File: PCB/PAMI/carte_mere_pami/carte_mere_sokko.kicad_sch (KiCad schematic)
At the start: 36 parts, among them IC1 ESP32-S3-WROOM-1-N16R8, IC2 LDO_3.3V_bis, J1 Conn_01x08_Socket, J10 Conn_01x07_Socket, J11 Conn_01x07_Socket, J12 Conn_Servos, J13 Unused GPIO Pins, J14 LiDAR Connector, J2 Connector 5V, J3 Connector 3.3V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

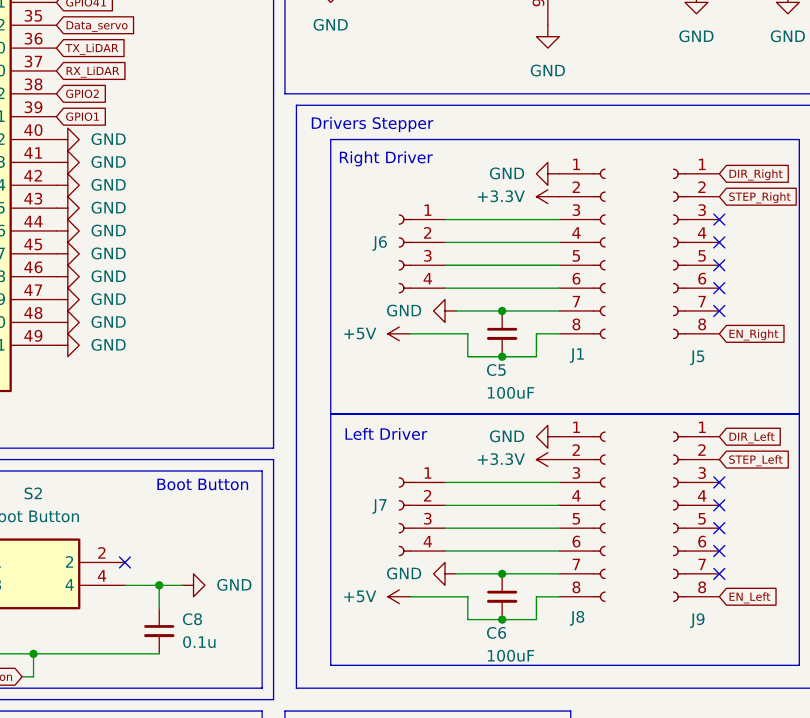
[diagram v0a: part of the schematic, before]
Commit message: PCB PAMI Nearly done, lack ground plane
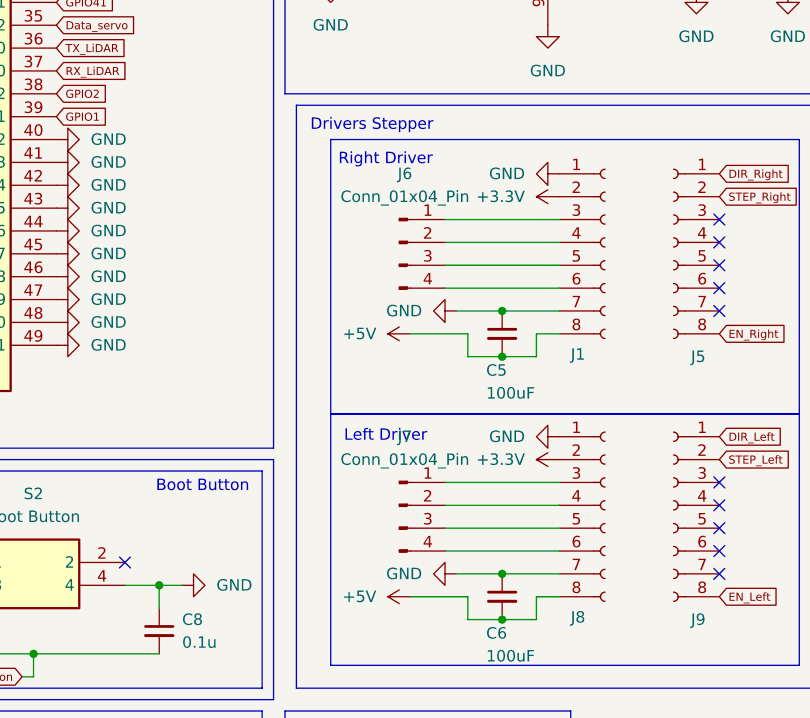
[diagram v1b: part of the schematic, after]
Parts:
- removed J6, J7: Conn_01x04_Socket, Connector_PinHeader_2.54mm:PinHeader_1x04_P2.54mm_Vertical, symbol Connector:Conn_01x04_Socket
- added J6, J7: Conn_01x04_Pin, Connector_JST:JST_XH_B4B-XH-A_1x04_P2.50mm_Vertical, symbol Connector:Conn_01x04_Pin
- J13: now left out of the parts list
- R2: footprint (none) -> Resistor_SMD:R_0805_2012Metric_Pad1.20x1.40mm_HandSolder
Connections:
- net at J8.3 (Pin_3): now also J7.1 (Pin_1)
- net at J8.4 (Pin_4): now also J7.2 (Pin_2)
- net at J8.5 (Pin_5): now also J7.3 (Pin_3)
- net at J8.6 (Pin_6): now also J7.4 (Pin_4)
- net at J1.3 (Pin_3): now also J6.1 (Pin_1)
- net at J1.4 (Pin_4): now also J6.2 (Pin_2)
- net at J1.5 (Pin_5): now also J6.3 (Pin_3)
- net at J1.6 (Pin_6): now also J6.4 (Pin_4)
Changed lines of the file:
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@@
 		(unit 1)
 		(exclude_from_sim no)
-		(in_bom yes)
-		(on_board yes)
+		(in_bom no)
+		(on_board no)
 		(dnp no)
 		(property "Reference" "J13"
@@
 	)
 	(symbol
-		(lib_id "Connector:Conn_01x04_Socket")
-		(at 378.46 137.16 0)
-		(mirror y)
+		(lib_id "power:GND")
+		(at 148.59 203.2 0)
 		(unit 1)
 		(exclude_from_sim no)
@@
 		(on_board yes)
 		(dnp no)
-		(property "Reference" "J6"
-			(at 377.19 137.1599 0)
+		(property "Reference" "#PWR023"
+			(at 148.59 209.55 0)
 			(effects
 				(font
 					(size 1.27 1.27)
 				)
-				(justify left)
+				(hide yes)
 			)
 		)
-		(property "Value" "Conn_01x04_Socket"
-			(at 377.19 139.6999 0)
+		(property "Value" "GND"
+			(at 149.098 207.772 0)
 			(effects
 				(font
 					(size 1.27 1.27)
 				)
-				(justify left)
-				(hide yes)
 			)
 		)
-		(property "Footprint" "Connector_PinHeader_2.54mm:PinHeader_1x04_P2.54mm_Vertical"
-			(at 378.46 137.16 0)
+		(property "Footprint" ""
+			(at 148.59 203.2 0)
 			(effects
 				(font
@@
 			)
 		)
-		(property "Datasheet" "~"
-			(at 378.46 137.16 0)
+		(property "Datasheet" ""
+			(at 148.59 203.2 0)
 			(effects
 				(font
@@
 			)
 		)
-		(property "Description" "Generic connector, single row, 01x04, script generated"
-			(at 378.46 137.16 0)
+		(property "Description" "Power symbol creates a global label with name \"GND\" , ground"
+			(at 148.59 203.2 0)
 			(effects
 				(font
@@
 			)
 		)
-		(pin "2"
-		)
-		(pin "4"
-		)
-		(pin "3"
-		)
 		(pin "1"
 		)
 		(instances
-			(project ""
+			(project "carte_mere_sokko"
 				(path "/dee43b08-90b1-40b6-8660-52baa7e8ef70"
-					(reference "J6")
+					(reference "#PWR023")
 					(unit 1)
 				)
@@
 	)
 	(symbol
-		(lib_id "power:GND")
-		(at 148.59 203.2 0)
+		(lib_id "power:+3.3V")
+		(at 396.24 132.08 90)
 		(unit 1)
 		(exclude_from_sim no)
@@
 		(on_board yes)
 		(dnp no)
-		(property "Reference" "#PWR023"
-			(at 148.59 209.55 0)
+		(fields_autoplaced yes)
+		(property "Reference" "#PWR013"
+			(at 400.05 132.08 0)
 			(effects
 				(font
@@
 			)
 		)
-		(property "Value" "GND"
-			(at 149.098 207.772 0)
+		(property "Value" "+3.3V"
+			(at 392.43 132.0799 90)
 			(effects
 				(font
 					(size 1.27 1.27)
 				)
+				(justify left)
 			)
 		)
 		(property "Footprint" ""
-			(at 148.59 203.2 0)
+			(at 396.24 132.08 0)
 			(effects
 				(font
@@
 		)
 		(property "Datasheet" ""
-			(at 148.59 203.2 0)
+			(at 396.24 132.08 0)
 			(effects
 				(font
@@
 			)
 		)
-		(property "Description" "Power symbol creates a global label with name \"GND\" , ground"
-			(at 148.59 203.2 0)
+		(property "Description" "Power symbol creates a global label with name \"+3.3V\""
+			(at 396.24 132.08 0)
 			(effects
 				(font
@@
 			(project "carte_mere_sokko"
 				(path "/dee43b08-90b1-40b6-8660-52baa7e8ef70"
-					(reference "#PWR023")
+					(reference "#PWR013")
 					(unit 1)
 				)
@@
 	)
 	(symbol
-		(lib_id "power:+3.3V")
-		(at 396.24 132.08 90)
+		(lib_id "Connector:Conn_01x04_Pin")
+		(at 378.46 166.37 0)
 		(unit 1)
 		(exclude_from_sim no)
@@
 		(dnp no)
 		(fields_autoplaced yes)
-		(property "Reference" "#PWR013"
-			(at 400.05 132.08 0)
+		(property "Reference" "J7"
+			(at 379.095 158.75 0)
 			(effects
 				(font
 					(size 1.27 1.27)
 				)
-				(hide yes)
 			)
 		)
-		(property "Value" "+3.3V"
-			(at 392.43 132.0799 90)
+		(property "Value" "Conn_01x04_Pin"
+			(at 379.095 161.29 0)
 			(effects
 				(font
 					(size 1.27 1.27)
 				)
-				(justify left)
 			)
 		)
-		(property "Footprint" ""
-			(at 396.24 132.08 0)
+		(property "Footprint" "Connector_JST:JST_XH_B4B-XH-A_1x04_P2.50mm_Vertical"
+			(at 378.46 166.37 0)
 			(effects
 				(font
@@
 			)
 		)
-		(property "Datasheet" ""
-			(at 396.24 132.08 0)
+		(property "Datasheet" "~"
+			(at 378.46 166.37 0)
 			(effects
 				(font
@@
 			)
 		)
-		(property "Description" "Power symbol creates a global label with name \"+3.3V\""
-			(at 396.24 132.08 0)
+		(property "Description" "Generic connector, single row, 01x04, script generated"
+			(at 378.46 166.37 0)
 			(effects
 				(font
@@
 		(pin "1"
 		)
+		(pin "2"
+		)
+		(pin "3"
+		)
+		(pin "4"
+		)
 		(instances
-			(project "carte_mere_sokko"
+			(project ""
 				(path "/dee43b08-90b1-40b6-8660-52baa7e8ef70"
-					(reference "#PWR013")
+					(reference "J7")
 					(unit 1)
 				)
@@
 	)
 	(symbol
+		(lib_id "Connector:Conn_01x04_Pin")
+		(at 378.46 137.16 0)
+		(unit 1)
+		(exclude_from_sim no)
+		(in_bom yes)
+		(on_board yes)
+		(dnp no)
+		(fields_autoplaced yes)
+		(property "Reference" "J6"
+			(at 379.095 129.54 0)
+			(effects
+				(font
+					(size 1.27 1.27)
+				)
+			)
+		)
+		(property "Value" "Conn_01x04_Pin"
+			(at 379.095 132.08 0)
+			(effects
+				(font
+					(size 1.27 1.27)
+				)
+			)
+		)
+		(property "Footprint" "Connector_JST:JST_XH_B4B-XH-A_1x04_P2.50mm_Vertical"
+			(at 378.46 137.16 0)
+			(effects
+				(font
+					(size 1.27 1.27)
+				)
+				(hide yes)
+			)
+		)
+		(property "Datasheet" "~"
+			(at 378.46 137.16 0)
+			(effects
+				(font
+					(size 1.27 1.27)
+				)
+				(hide yes)
+			)
+		)
+		(property "Description" "Generic connector, single row, 01x04, script generated"
+			(at 378.46 137.16 0)
+			(effects
+				(font
+					(size 1.27 1.27)
+				)
+				(hide yes)
+			)
+		)
+		(pin "2"
+		)
+		(pin "4"
+		)
+		(pin "3"
+		)
+		(pin "1"
+		)
+		(instances
+			(project ""
+				(path "/dee43b08-90b1-40b6-8660-52baa7e8ef70"
+					(reference "J6")
+					(unit 1)
+				)
+			)
+		)
+	)
+	(symbol
 		(lib_id "power:GND")
 		(at 384.81 144.78 270)
@@
 			)
 		)
-		(property "Footprint" ""
+		(property "Footprint" "Resistor_SMD:R_0805_2012Metric_Pad1.20x1.40mm_HandSolder"
 			(at 285.242 109.22 90)
 			(effects
@@
 					(unit 1)
 				)
-			)
-		)
-	)
-	(symbol
-		(lib_id "Connector:Conn_01x04_Socket")
-		(at 378.46 166.37 0)
-		(mirror y)
-		(unit 1)
-		(exclude_from_sim no)
-		(in_bom yes)
-		(on_board yes)
-		(dnp no)
-		(property "Reference" "J7"
-			(at 377.19 166.3699 0)
-			(effects
-				(font
-					(size 1.27 1.27)
-				)
-				(justify left)
-			)
-		)
-		(property "Value" "Conn_01x04_Socket"
-			(at 377.19 168.9099 0)
-			(effects
-				(font
-					(size 1.27 1.27)
-				)
-				(justify left)
-				(hide yes)
-			)
-		)
-		(property "Footprint" "Connector_PinHeader_2.54mm:PinHeader_1x04_P2.54mm_Vertical"
-			(at 378.46 166.37 0)
-			(effects
-				(font
-					(size 1.27 1.27)
-				)
-				(hide yes)
-			)
-		)
-		(property "Datasheet" "~"
-			(at 378.46 166.37 0)
-			(effects
-				(font
-					(size 1.27 1.27)
-				)
-				(hide yes)
-			)
-		)
-		(property "Description" "Generic connector, single row, 01x04, script generated"
-			(at 378.46 166.37 0)
-			(effects
-				(font
-					(size 1.27 1.27)
-				)
-				(hide yes)
-			)
-		)
-		(pin "2"
-		)
-		(pin "4"
-		)
-		(pin "3"
-		)
-		(pin "1"
-		)
-		(instances
-			(project "carte_mere_sokko"
-				(path "/dee43b08-90b1-40b6-8660-52baa7e8ef70"
-					(reference "J7")
-					(unit 1)
-				)

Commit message: V2 PAMI Motherboard
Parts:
- J12: footprint Connector_JST:JST_XH_B3B-XH-A_1x03_P2.50mm_Vertical -> Connector_PinHeader_2.00mm:PinHeader_1x03_P2.00mm_Vertical
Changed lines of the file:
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@@
 			)
 		)
-		(property "Footprint" "Connector_JST:JST_XH_B3B-XH-A_1x03_P2.50mm_Vertical"
+		(property "Footprint" "Connector_PinHeader_2.00mm:PinHeader_1x03_P2.00mm_Vertical"
 			(at 375.92 200.66 0)
 			(effects

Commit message: biboup
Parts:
- removed C11: 1uF, Capacitor_SMD:C_0805_2012Metric_Pad1.18x1.45mm_HandSolder, symbol Device:C_Small
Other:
- moved on the sheet: R2
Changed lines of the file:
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@@
 	)
 	(junction
-		(at 287.02 105.41)
-		(diameter 0)
-		(color 0 0 0 0)
-	)
-	(junction
 		(at 389.89 149.86)
 		(diameter 0)
@@
 	)
 	(junction
+		(at 287.02 95.25)
+		(diameter 0)
+		(color 0 0 0 0)
+	)
+	(junction
 		(at 248.92 138.43)
 		(diameter 0)
@@
 	(wire
 		(pts
-			(xy 297.18 105.41) (xy 297.18 95.25)
-		)
-		(stroke
-			(width 0)
-			(type default)
-		)
-	)
-	(wire
-		(pts
 			(xy 383.54 168.91) (xy 396.24 168.91)
 		)
@@
 	(wire
 		(pts
-			(xy 287.02 105.41) (xy 297.18 105.41)
-		)
-		(stroke
-			(width 0)
-			(type default)
-		)
-	)
-	(wire
-		(pts
-			(xy 297.18 95.25) (xy 307.34 95.25)
+			(xy 281.94 95.25) (xy 287.02 95.25)
 		)
 		(stroke
@@
 	(wire
 		(pts
+			(xy 287.02 95.25) (xy 307.34 95.25)
+		)
+		(stroke
+			(width 0)
+			(type default)
+		)
+	)
+	(wire
+		(pts
 			(xy 378.46 81.28) (xy 392.43 81.28)
 		)
@@
 	(wire
 		(pts
-			(xy 345.44 213.36) (xy 350.52 213.36)
+			(xy 287.02 95.25) (xy 287.02 96.52)
 		)
 		(stroke
@@
 	(wire
 		(pts
-			(xy 370.84 106.68) (xy 370.84 107.95)
+			(xy 345.44 213.36) (xy 350.52 213.36)
 		)
 		(stroke
@@
 	(wire
 		(pts
-			(xy 370.84 106.68) (xy 378.46 106.68)
+			(xy 370.84 106.68) (xy 370.84 107.95)
 		)
 		(stroke
@@
 	(wire
 		(pts
-			(xy 414.02 99.06) (xy 414.02 100.33)
+			(xy 370.84 106.68) (xy 378.46 106.68)
 		)
 		(stroke
@@
 	(wire
 		(pts
-			(xy 289.56 86.36) (xy 289.56 87.63)
+			(xy 414.02 99.06) (xy 414.02 100.33)
 		)
 		(stroke
@@
 	(wire
 		(pts
-			(xy 370.84 105.41) (xy 370.84 106.68)
+			(xy 289.56 86.36) (xy 289.56 87.63)
 		)
 		(stroke
@@
 	(wire
 		(pts
-			(xy 281.94 105.41) (xy 287.02 105.41)
+			(xy 370.84 105.41) (xy 370.84 106.68)
 		)
 		(stroke
@@
 	(wire
 		(pts
-			(xy 287.02 114.3) (xy 287.02 113.03)
-		)
-		(stroke
-			(width 0)
-			(type default)
-		)
-	)
-	(wire
-		(pts
 			(xy 284.48 86.36) (xy 280.67 86.36)
 		)
@@
 	(global_label "Enable_BTN"
 		(shape input)
-		(at 281.94 105.41 180)
+		(at 281.94 95.25 180)
 		(fields_autoplaced yes)
 		(effects
@@
 		)
 		(property "Intersheetrefs" "${INTERSHEET_REFS}"
-			(at 272.1104 105.41 0)
+			(at 272.1104 95.25 0)
 			(effects
 				(font
@@
 	(symbol
 		(lib_id "power:+3.3V")
-		(at 287.02 114.3 90)
+		(at 287.02 104.14 90)
 		(unit 1)
 		(exclude_from_sim no)
@@
 		(fields_autoplaced yes)
 		(property "Reference" "#PWR046"
-			(at 290.83 114.3 0)
+			(at 290.83 104.14 0)
 			(effects
 				(font
@@
 		)
 		(property "Value" "+3.3V"
-			(at 283.21 114.2999 90)
+			(at 283.21 104.1399 90)
 			(effects
 				(font
@@
 		)
 		(property "Footprint" ""
-			(at 287.02 114.3 0)
+			(at 287.02 104.14 0)
 			(effects
 				(font
@@
 		)
 		(property "Datasheet" ""
-			(at 287.02 114.3 0)
+			(at 287.02 104.14 0)
 			(effects
 				(font
@@
 		)
 		(property "Description" "Power symbol creates a global label with name \"+3.3V\""
-			(at 287.02 114.3 0)
+			(at 287.02 104.14 0)
 			(effects
 				(font
@@
 	(symbol
 		(lib_id "Device:R")
-		(at 287.02 109.22 0)
+		(at 287.02 100.33 0)
 		(unit 1)
 		(exclude_from_sim no)
@@
 		(fields_autoplaced yes)
 		(property "Reference" "R2"
-			(at 289.56 107.9499 0)
+			(at 289.56 99.0599 0)
 			(effects
 				(font
@@
 		)
 		(property "Value" "10k"
-			(at 289.56 110.4899 0)
+			(at 289.56 101.5999 0)
 			(effects
 				(font
@@
 		)
 		(property "Footprint" "Resistor_SMD:R_0805_2012Metric_Pad1.20x1.40mm_HandSolder"
-			(at 285.242 109.22 90)
+			(at 285.242 100.33 90)
 			(effects
 				(font
@@
 		)
 		(property "Datasheet" "~"
-			(at 287.02 109.22 0)
+			(at 287.02 100.33 0)
 			(effects
 				(font
@@
 		)
 		(property "Description" "Resistor"
-			(at 287.02 109.22 0)
+			(at 287.02 100.33 0)
 			(effects
 				(font
@@
 	)
 	(symbol
-		(lib_id "Device:C_Small")
-		(at 287.02 102.87 0)
-		(unit 1)
-		(exclude_from_sim no)
-		(in_bom yes)
-		(on_board yes)
-		(dnp no)
-		(fields_autoplaced yes)
-		(property "Reference" "C11"
-			(at 289.56 101.6062 0)
-			(effects
-				(font
-					(size 1.27 1.27)
-				)
-				(justify left)
-			)
-		)
-		(property "Value" "1uF"
-			(at 289.56 104.1462 0)
-			(effects
-				(font
-					(size 1.27 1.27)
-				)
-				(justify left)
-			)
-		)
-		(property "Footprint" "Capacitor_SMD:C_0805_2012Metric_Pad1.18x1.45mm_HandSolder"
-			(at 287.02 102.87 0)
-			(effects
-				(font
-					(size 1.27 1.27)
-				)
-				(hide yes)
-			)
-		)
-		(property "Datasheet" "~"
-			(at 287.02 102.87 0)
-			(effects
-				(font
-					(size 1.27 1.27)
-				)
-				(hide yes)
-			)
-		)
-		(property "Description" "Unpolarized capacitor, small symbol"
-			(at 287.02 102.87 0)
-			(effects
-				(font
-					(size 1.27 1.27)
-				)
-				(hide yes)
-			)
-		)
-		(pin "2"
-		)
-		(pin "1"
-		)
-		(instances
-			(project "carte_mere_sokko"
-				(path "/dee43b08-90b1-40b6-8660-52baa7e8ef70"
-					(reference "C11")
-					(unit 1)
-				)
-			)
-		)
-	)
-	(symbol
 		(lib_id "power:+3.3V")
 		(at 293.37 200.66 180)
@@
 					(unit 1)
 				)
-			)
-		)
-	)
-	(symbol
-		(lib_id "power:GND")
-		(at 287.02 100.33 0)
-		(mirror x)
-		(unit 1)
-		(exclude_from_sim no)
-		(in_bom yes)
-		(on_board yes)
-		(dnp no)
-		(property "Reference" "#PWR047"
-			(at 287.02 93.98 0)
-			(effects
-				(font
-					(size 1.27 1.27)
-				)
-				(hide yes)
-			)
-		)
-		(property "Value" "GND"
-			(at 287.02 95.25 0)
-			(effects
-				(font
-					(size 1.27 1.27)
-				)
-			)
-		)
-		(property "Footprint" ""
-			(at 287.02 100.33 0)
-			(effects
-				(font
-					(size 1.27 1.27)
-				)
-				(hide yes)
-			)
-		)
-		(property "Datasheet" ""
-			(at 287.02 100.33 0)
-			(effects
-				(font
-					(size 1.27 1.27)
-				)
-				(hide yes)
-			)
-		)
-		(property "Description" "Power symbol creates a global label with name \"GND\" , ground"
-			(at 287.02 100.33 0)
-			(effects
-				(font
-					(size 1.27 1.27)
-				)
-				(hide yes)
-			)
-		)
-		(pin "1"
-		)
-		(instances
-			(project "carte_mere_sokko"
-				(path "/dee43b08-90b1-40b6-8660-52baa7e8ef70"
-					(reference "#PWR047")
-					(unit 1)
-				)
